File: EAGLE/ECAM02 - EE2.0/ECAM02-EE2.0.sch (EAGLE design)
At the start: 61 parts, among them J1 MODULAR TOOL, J2 SPI, J3 MOT, J4 FTDI, J5 S4B-PH-SM4, J6 SOL+PUMP, J7 RINGLIGHT, Q2 16MHz, U1 SP3485, U10 MCP4725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

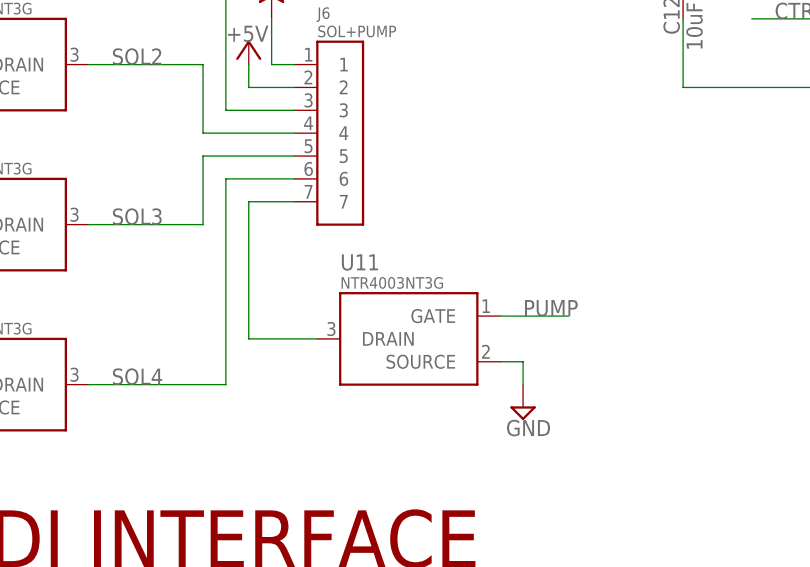
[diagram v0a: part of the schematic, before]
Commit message: Fixed BOM, began adding DFM changes
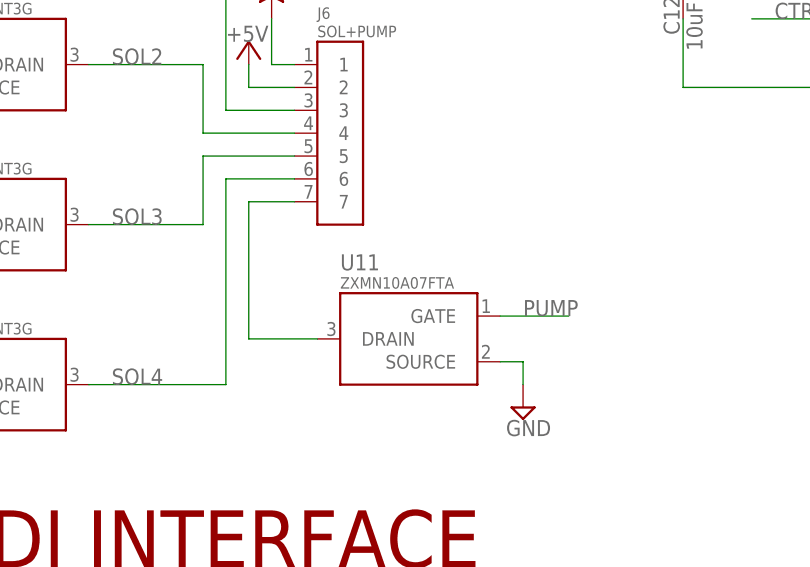
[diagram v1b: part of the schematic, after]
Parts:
- U11: value NTR4003NT3G -> ZXMN10A07FTA; device TinWhiskers:CPL-MOSFET-NCH-SOT23 -> TinWhiskers:CPL-MOSFET-NCH-SOT23ZXMN10A07FTA; PARTNO NTR4003NT3G -> ZXMN10A07FTA
- U4, U5, U6, U7: device TinWhiskers:CPL-MOSFET-NCH-SOT23 -> TinWhiskers:CPL-MOSFET-NCH-SOT23NTR4003N
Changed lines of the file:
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@@
 <?xml version="1.0" encoding="utf-8"?>
 <!DOCTYPE eagle SYSTEM "eagle.dtd">
-<eagle version="7.3.0">
+<eagle version="7.4.0">
 <drawing>
 <settings>
@@
 <part name="SUPPLY18" library="TinWhiskers" deviceset="GND" device=""/>
 <part name="SUPPLY19" library="TinWhiskers" deviceset="GND" device=""/>
-<part name="U4" library="TinWhiskers" deviceset="CPL-MOSFET-NCH-SOT23" device="" value="NTR4003NT3G">
+<part name="U4" library="TinWhiskers" deviceset="CPL-MOSFET-NCH-SOT23" device="NTR4003N" value="NTR4003NT3G">
 <attribute name="PARTNO" value="NTR4003NT3G"/>
 </part>
-<part name="U5" library="TinWhiskers" deviceset="CPL-MOSFET-NCH-SOT23" device="" value="NTR4003NT3G">
+<part name="U5" library="TinWhiskers" deviceset="CPL-MOSFET-NCH-SOT23" device="NTR4003N" value="NTR4003NT3G">
 <attribute name="PARTNO" value="NTR4003NT3G"/>
 </part>
-<part name="U6" library="TinWhiskers" deviceset="CPL-MOSFET-NCH-SOT23" device="" value="NTR4003NT3G">
+<part name="U6" library="TinWhiskers" deviceset="CPL-MOSFET-NCH-SOT23" device="NTR4003N" value="NTR4003NT3G">
 <attribute name="PARTNO" value="NTR4003NT3G"/>
 </part>
-<part name="U7" library="TinWhiskers" deviceset="CPL-MOSFET-NCH-SOT23" device="" value="NTR4003NT3G">
+<part name="U7" library="TinWhiskers" deviceset="CPL-MOSFET-NCH-SOT23" device="NTR4003N" value="NTR4003NT3G">
 <attribute name="PARTNO" value="NTR4003NT3G"/>
 </part>
@@
 <attribute name="PARTNO" value="B7B-PH-SM4-TB(LF)(SN)"/>
 </part>
-<part name="U11" library="TinWhiskers" deviceset="CPL-MOSFET-NCH-SOT23" device="" value="NTR4003NT3G">
-<attribute name="PARTNO" value="NTR4003NT3G"/>
+<part name="U11" library="TinWhiskers" deviceset="CPL-MOSFET-NCH-SOT23" device="ZXMN10A07FTA" value="ZXMN10A07FTA">
+<attribute name="PARTNO" value="ZXMN10A07FTA"/>
 </part>
 <part name="SUPPLY32" library="TinWhiskers" deviceset="GND" device=""/>

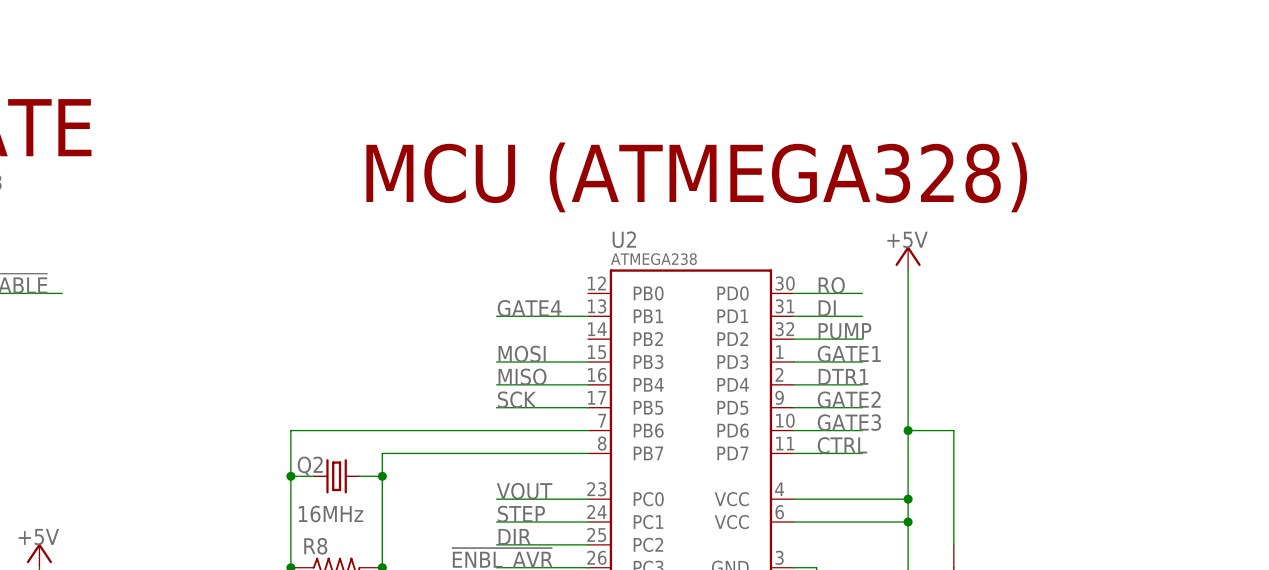
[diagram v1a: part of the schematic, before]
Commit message: Made REV 2 modifications, including increasing width of power traces, adding vias to power traces, and addition of LEDs to all modular tools. Catch diodes added to ESOL01 board to prevent coils from creating problems "upstream"
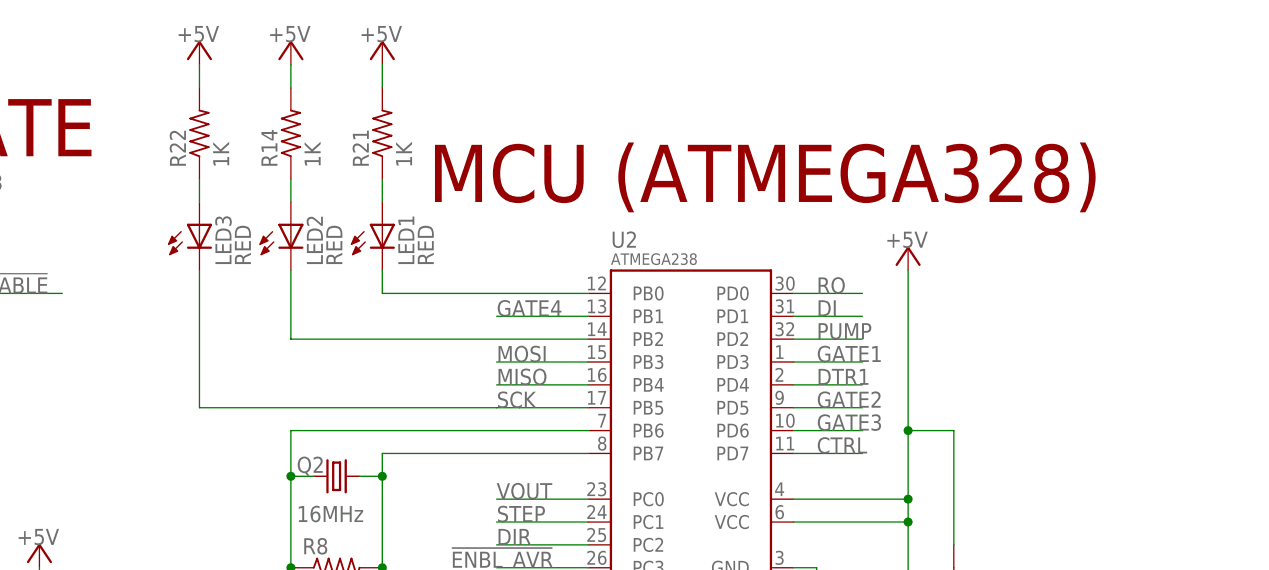
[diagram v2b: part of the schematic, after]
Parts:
- added LED1, LED2, LED3: RED, TinWhiskers:CPL-LED-0603-RED
- added R14, R21, R22: 1K, TinWhiskers:CPL-RES-0603-1K-0.1W
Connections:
- new net N$1: LED1.A, R21.1
- new net N$11: LED3.A, R22.1
- new net N$2: LED2.A, R14.1
- new net N$3: LED1.C, U2.PB0
- new net N$4: LED2.C, U2.PB2
- net +5V: now also R14.2, R21.2, R22.2
- net SCK: now also LED3.C
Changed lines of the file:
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@@
 <part name="SUPPLY36" library="TinWhiskers" deviceset="GND" device=""/>
 <part name="SUPPLY37" library="TinWhiskers" deviceset="GND" device=""/>
+<part name="LED1" library="TinWhiskers" deviceset="CPL-LED-0603-RED" device="" value="RED"/>
+<part name="LED2" library="TinWhiskers" deviceset="CPL-LED-0603-RED" device="" value="RED"/>
+<part name="R14" library="TinWhiskers" deviceset="CPL-RES-0603-1K-0.1W" device="" value="1K"/>
+<part name="R21" library="TinWhiskers" deviceset="CPL-RES-0603-1K-0.1W" device="" value="1K"/>
+<part name="P+18" library="supply1" deviceset="+5V" device=""/>
+<part name="P+19" library="supply1" deviceset="+5V" device=""/>
+<part name="LED3" library="TinWhiskers" deviceset="CPL-LED-0603-RED" device="" value="RED"/>
+<part name="R22" library="TinWhiskers" deviceset="CPL-RES-0603-1K-0.1W" device="" value="1K"/>
+<part name="P+20" library="supply1" deviceset="+5V" device=""/>
 </parts>
 <sheets>
@@
 <text x="292.1" y="10.16" size="2.54" layer="94" ratio="10">REVISION:</text>
 <text x="20.32" y="101.6" size="6.35" layer="94" ratio="10">RS-485 INTERFACE</text>
-<text x="292.1" y="236.22" size="6.35" layer="94" ratio="10">MCU (ATMEGA328)</text>
+<text x="299.72" y="236.22" size="6.35" layer="94" ratio="10">MCU (ATMEGA328)</text>
 <text x="210.82" y="101.6" size="6.35" layer="94" ratio="10">V-REG (5V-3.3V)</text>
 <text x="17.78" y="154.94" size="6.35" layer="94" ratio="10">FTDI INTERFACE</text>
@@
 <attribute name="VALUE" x="170.815" y="121.285" size="1.778" layer="96"/>
 </instance>
+<instance part="LED1" gate="G$1" x="294.64" y="233.68"/>
+<instance part="LED2" gate="G$1" x="284.48" y="233.68"/>
+<instance part="R14" gate="G$1" x="284.48" y="243.84" rot="R90"/>
+<instance part="R21" gate="G$1" x="294.64" y="243.84" rot="R90"/>
+<instance part="P+18" gate="1" x="284.48" y="254" smashed="yes">
+<attribute name="VALUE" x="281.94" y="254" size="1.778" layer="96"/>
+</instance>
+<instance part="P+19" gate="1" x="294.64" y="254" smashed="yes">
+<attribute name="VALUE" x="292.1" y="254" size="1.778" layer="96"/>
+</instance>
+<instance part="LED3" gate="G$1" x="274.32" y="233.68"/>
+<instance part="R22" gate="G$1" x="274.32" y="243.84" rot="R90"/>
+<instance part="P+20" gate="1" x="274.32" y="254" smashed="yes">
+<attribute name="VALUE" x="271.78" y="254" size="1.778" layer="96"/>
+</instance>
 </instances>
 <busses>
@@
 <wire x1="256.54" y1="195.58" x2="256.54" y2="193.04" width="0.1524" layer="91"/>
 </segment>
+<segment>
+<pinref part="P+18" gate="1" pin="+5V"/>
+<pinref part="R14" gate="G$1" pin="2"/>
+<wire x1="284.48" y1="251.46" x2="284.48" y2="248.92" width="0.1524" layer="91"/>
+</segment>
+<segment>
+<pinref part="P+19" gate="1" pin="+5V"/>
+<pinref part="R21" gate="G$1" pin="2"/>
+<wire x1="294.64" y1="251.46" x2="294.64" y2="248.92" width="0.1524" layer="91"/>
+</segment>
+<segment>
+<pinref part="P+20" gate="1" pin="+5V"/>
+<pinref part="R22" gate="G$1" pin="2"/>
+<wire x1="274.32" y1="251.46" x2="274.32" y2="248.92" width="0.1524" layer="91"/>
+</segment>
 </net>
 <net name="A" class="0">
@@
 <segment>
 <pinref part="U2" gate="G$1" pin="PB5"/>
-<wire x1="317.5" y1="213.36" x2="307.34" y2="213.36" width="0.1524" layer="91"/>
+<wire x1="317.5" y1="213.36" x2="309.88" y2="213.36" width="0.1524" layer="91"/>
 <label x="307.34" y="213.36" size="1.778" layer="95" ratio="12"/>
+<pinref part="LED3" gate="G$1" pin="C"/>
+<wire x1="309.88" y1="213.36" x2="307.34" y2="213.36" width="0.1524" layer="91"/>
+<wire x1="274.32" y1="228.6" x2="274.32" y2="213.36" width="0.1524" layer="91"/>
+<wire x1="274.32" y1="213.36" x2="307.34" y2="213.36" width="0.1524" layer="91"/>
 </segment>
 <segment>
@@
 <segment>
 <pinref part="U5" gate="G$1" pin="DRAIN"/>
+<label x="40.64" y="210.82" size="1.778" layer="95"/>
 <wire x1="38.1" y1="210.82" x2="50.8" y2="210.82" width="0.1524" layer="91"/>
-<label x="40.64" y="210.82" size="1.778" layer="95"/>
 <wire x1="60.96" y1="203.2" x2="50.8" y2="203.2" width="0.1524" layer="91"/>
 <wire x1="50.8" y1="203.2" x2="50.8" y2="210.82" width="0.1524" layer="91"/>
@@
 <segment>
 <pinref part="U6" gate="G$1" pin="DRAIN"/>
+<label x="40.64" y="193.04" size="1.778" layer="95"/>
 <wire x1="38.1" y1="193.04" x2="50.8" y2="193.04" width="0.1524" layer="91"/>
-<label x="40.64" y="193.04" size="1.778" layer="95"/>
 <wire x1="60.96" y1="200.66" x2="50.8" y2="200.66" width="0.1524" layer="91"/>
 <wire x1="50.8" y1="200.66" x2="50.8" y2="193.04" width="0.1524" layer="91"/>
@@
 </segment>
 </net>
+<net name="N$1" class="0">
+<segment>
+<pinref part="R21" gate="G$1" pin="1"/>
+<pinref part="LED1" gate="G$1" pin="A"/>
+<wire x1="294.64" y1="238.76" x2="294.64" y2="236.22" width="0.1524" layer="91"/>
+</segment>
+</net>
+<net name="N$2" class="0">
+<segment>
+<pinref part="R14" gate="G$1" pin="1"/>
+<pinref part="LED2" gate="G$1" pin="A"/>
+<wire x1="284.48" y1="238.76" x2="284.48" y2="236.22" width="0.1524" layer="91"/>
+</segment>
+</net>
+<net name="N$3" class="0">
+<segment>
+<pinref part="U2" gate="G$1" pin="PB0"/>
+<pinref part="LED1" gate="G$1" pin="C"/>
+<wire x1="317.5" y1="226.06" x2="294.64" y2="226.06" width="0.1524" layer="91"/>
+<wire x1="294.64" y1="226.06" x2="294.64" y2="228.6" width="0.1524" layer="91"/>
+</segment>
+</net>
+<net name="N$4" class="0">
+<segment>
+<pinref part="U2" gate="G$1" pin="PB2"/>
+<pinref part="LED2" gate="G$1" pin="C"/>
+<wire x1="317.5" y1="220.98" x2="284.48" y2="220.98" width="0.1524" layer="91"/>
+<wire x1="284.48" y1="220.98" x2="284.48" y2="228.6" width="0.1524" layer="91"/>
+</segment>
+</net>
+<net name="N$11" class="0">
+<segment>
+<pinref part="R22" gate="G$1" pin="1"/>
+<pinref part="LED3" gate="G$1" pin="A"/>
+<wire x1="274.32" y1="238.76" x2="274.32" y2="236.22" width="0.1524" layer="91"/>
+</segment>
+</net>

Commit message: Fixed electrolytic cap reversals on ECAM02
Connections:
- net +24V: now also C17.POS; no longer C17.NEG
- net +5V: now also C18.POS; no longer C18.NEG
- net GND: now also C17.NEG, C18.NEG; no longer C17.POS, C18.POS
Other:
- moved on the sheet: C17, C18
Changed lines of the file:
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@@
 </instance>
 <instance part="SUPPLY34" gate="GND" x="210.82" y="218.44"/>
-<instance part="C17" gate="G$1" x="281.94" y="139.7" smashed="yes" rot="R90">
-<attribute name="NAME" x="281.559" y="133.096" size="1.778" layer="95" rot="R90"/>
-<attribute name="VALUE" x="284.099" y="130.81" size="1.778" layer="96" rot="R90"/>
-<attribute name="PARTNO" x="281.94" y="139.7" size="1.778" layer="96" display="off"/>
+<instance part="C17" gate="G$1" x="281.94" y="139.7" smashed="yes" rot="R270">
+<attribute name="NAME" x="281.559" y="133.858" size="1.778" layer="95" rot="R90"/>
+<attribute name="VALUE" x="284.099" y="130.556" size="1.778" layer="96" rot="R90"/>
+<attribute name="PARTNO" x="281.94" y="139.7" size="1.778" layer="96" rot="R180" display="off"/>
 </instance>
 <instance part="SUPPLY35" gate="GND" x="281.94" y="132.08"/>
-<instance part="C18" gate="G$1" x="256.54" y="190.5" smashed="yes" rot="R90">
+<instance part="C18" gate="G$1" x="256.54" y="190.5" smashed="yes" rot="R270">
 <attribute name="NAME" x="256.159" y="183.896" size="1.778" layer="95" rot="R90"/>
 <attribute name="VALUE" x="258.699" y="183.134" size="1.778" layer="96" rot="R90"/>
-<attribute name="PARTNO" x="256.54" y="190.5" size="1.778" layer="96" display="off"/>
+<attribute name="PARTNO" x="256.54" y="190.5" size="1.778" layer="96" rot="R180" display="off"/>
 </instance>
 <instance part="P+17" gate="1" x="256.54" y="198.12" smashed="yes">
@@
 </segment>
 <segment>
-<pinref part="C17" gate="G$1" pin="POS"/>
-<pinref part="SUPPLY35" gate="GND" pin="GND"/>
-<wire x1="281.94" y1="137.16" x2="281.94" y2="134.62" width="0.1524" layer="91"/>
-</segment>
-<segment>
-<pinref part="C18" gate="G$1" pin="POS"/>
-<pinref part="SUPPLY36" gate="GND" pin="GND"/>
-<wire x1="256.54" y1="187.96" x2="256.54" y2="182.88" width="0.1524" layer="91"/>
-</segment>
-<segment>
 <pinref part="U10" gate="G$1" pin="A0"/>
 <pinref part="SUPPLY37" gate="GND" pin="GND"/>
 <wire x1="160.02" y1="142.24" x2="172.72" y2="142.24" width="0.1524" layer="91"/>
 <wire x1="172.72" y1="142.24" x2="172.72" y2="127" width="0.1524" layer="91"/>
+</segment>
+<segment>
+<pinref part="C17" gate="G$1" pin="NEG"/>
+<pinref part="SUPPLY35" gate="GND" pin="GND"/>
+<wire x1="281.94" y1="137.16" x2="281.94" y2="134.62" width="0.1524" layer="91"/>
+</segment>
+<segment>
+<pinref part="C18" gate="G$1" pin="NEG"/>
+<pinref part="SUPPLY36" gate="GND" pin="GND"/>
+<wire x1="256.54" y1="187.96" x2="256.54" y2="182.88" width="0.1524" layer="91"/>
 </segment>
 </net>
@@
 <junction x="292.1" y="132.08"/>
 <pinref part="P+5" gate="1" pin="+24V"/>
-<pinref part="C17" gate="G$1" pin="NEG"/>
 <wire x1="292.1" y1="144.78" x2="292.1" y2="147.32" width="0.1524" layer="91"/>
 <wire x1="292.1" y1="144.78" x2="281.94" y2="144.78" width="0.1524" layer="91"/>
+<junction x="292.1" y="144.78"/>
+<pinref part="C17" gate="G$1" pin="POS"/>
 <wire x1="281.94" y1="144.78" x2="281.94" y2="142.24" width="0.1524" layer="91"/>
-<junction x="292.1" y="144.78"/>
 </segment>
 <segment>
@@
 </segment>
 <segment>
-<pinref part="P+17" gate="1" pin="+5V"/>
-<pinref part="C18" gate="G$1" pin="NEG"/>
-<wire x1="256.54" y1="195.58" x2="256.54" y2="193.04" width="0.1524" layer="91"/>
-</segment>
-<segment>
 <pinref part="P+18" gate="1" pin="+5V"/>
 <pinref part="R14" gate="G$1" pin="2"/>
@@
 <wire x1="274.32" y1="251.46" x2="274.32" y2="248.92" width="0.1524" layer="91"/>
 </segment>
+<segment>
+<pinref part="C18" gate="G$1" pin="POS"/>
+<pinref part="P+17" gate="1" pin="+5V"/>
+<wire x1="256.54" y1="193.04" x2="256.54" y2="195.58" width="0.1524" layer="91"/>
+</segment>
 </net>
